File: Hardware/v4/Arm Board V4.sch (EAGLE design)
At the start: 43 parts, among them IC3 L6206D, P1 STELLARIS-LAUNCHPADSTELLARIS-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, U1 SN74LS241DW, U2 XBEE-1B3

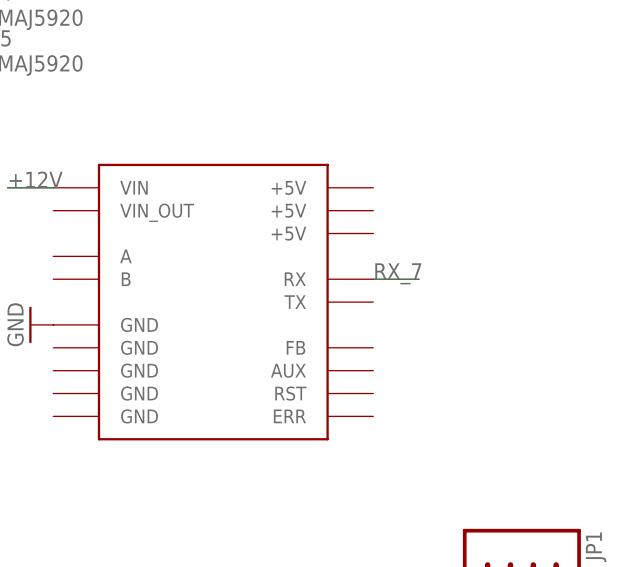
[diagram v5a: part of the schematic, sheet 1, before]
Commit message: fixed RX/TX issue between Tiva C and Pololu Jrk 21v3
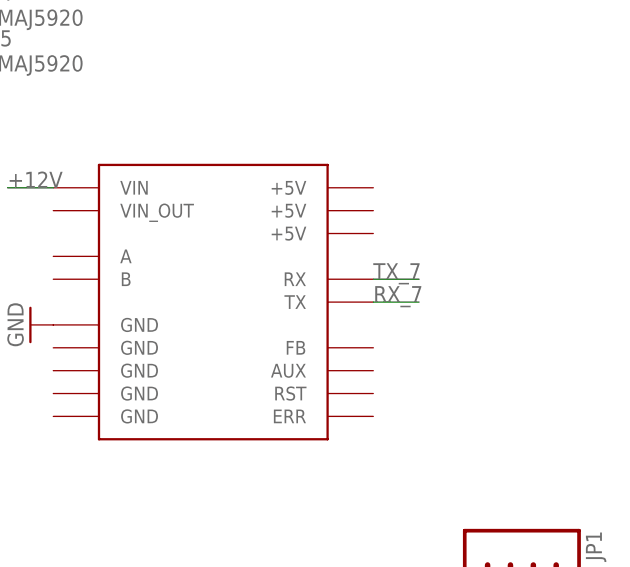
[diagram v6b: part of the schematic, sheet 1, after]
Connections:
- net RX_7: now also U$1.TX; no longer U$1.RX
- net TX_7: now also U$1.RX
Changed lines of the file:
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@@
 </segment>
 </net>
-<net name="RX_7" class="0">
+<net name="TX_7" class="0">
 <segment>
 <pinref part="U$1" gate="G$1" pin="RX"/>
@@
 </segment>
 </net>
+<net name="RX_7" class="0">
+<segment>
+<pinref part="U$1" gate="G$1" pin="TX"/>
+<wire x1="208.28" y1="10.16" x2="213.36" y2="10.16" width="0.1524" layer="91"/>
+<label x="208.28" y="10.16" size="1.778" layer="95"/>
+</segment>
+</net>
